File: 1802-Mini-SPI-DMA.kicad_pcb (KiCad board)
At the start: 2 copper layers, 100 x 100 mm, 44 parts, among them J1 Conn_02x05_Odd_Even, J2 Mount, J3 Mount, J4 Mount, J5 GRP_EXP, J6 Mount, J7 Conn_01x08, J8 GRP_SEL, J9 Expansion, U1 74HC04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

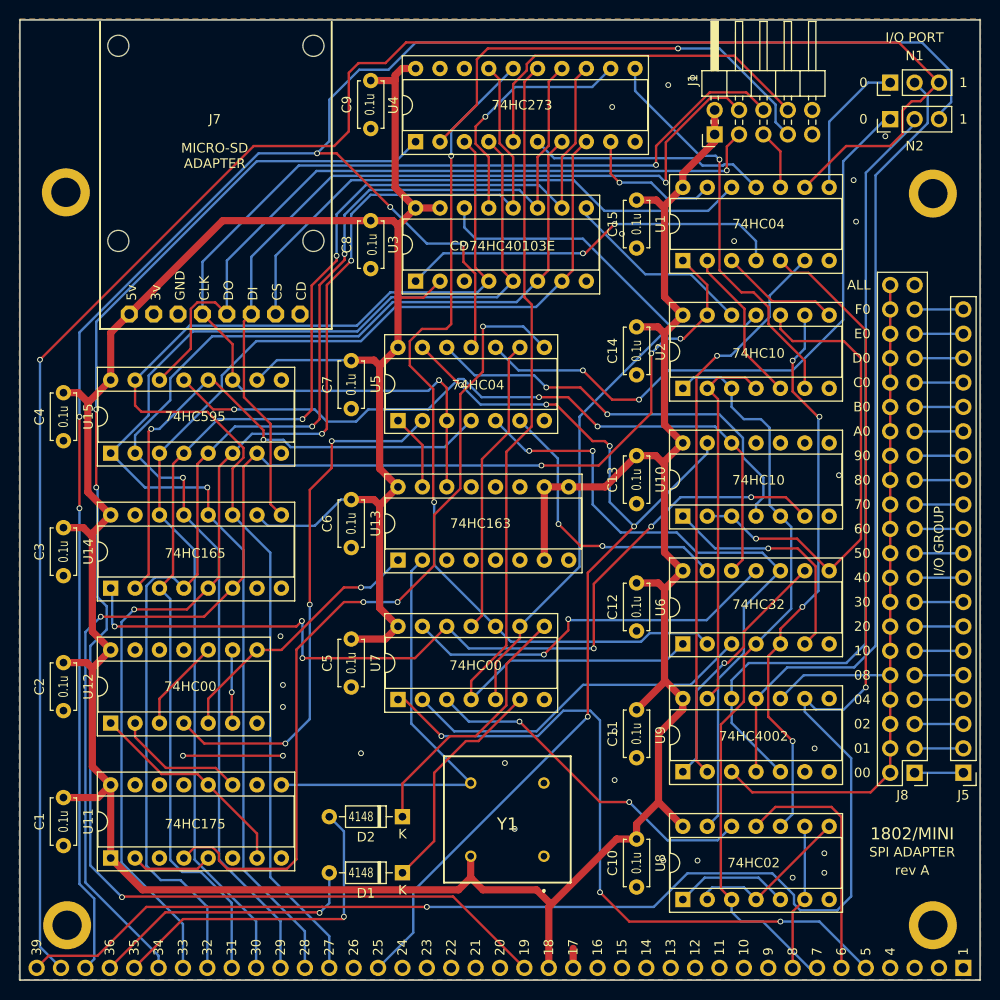
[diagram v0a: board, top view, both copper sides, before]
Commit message: Update silk screen.
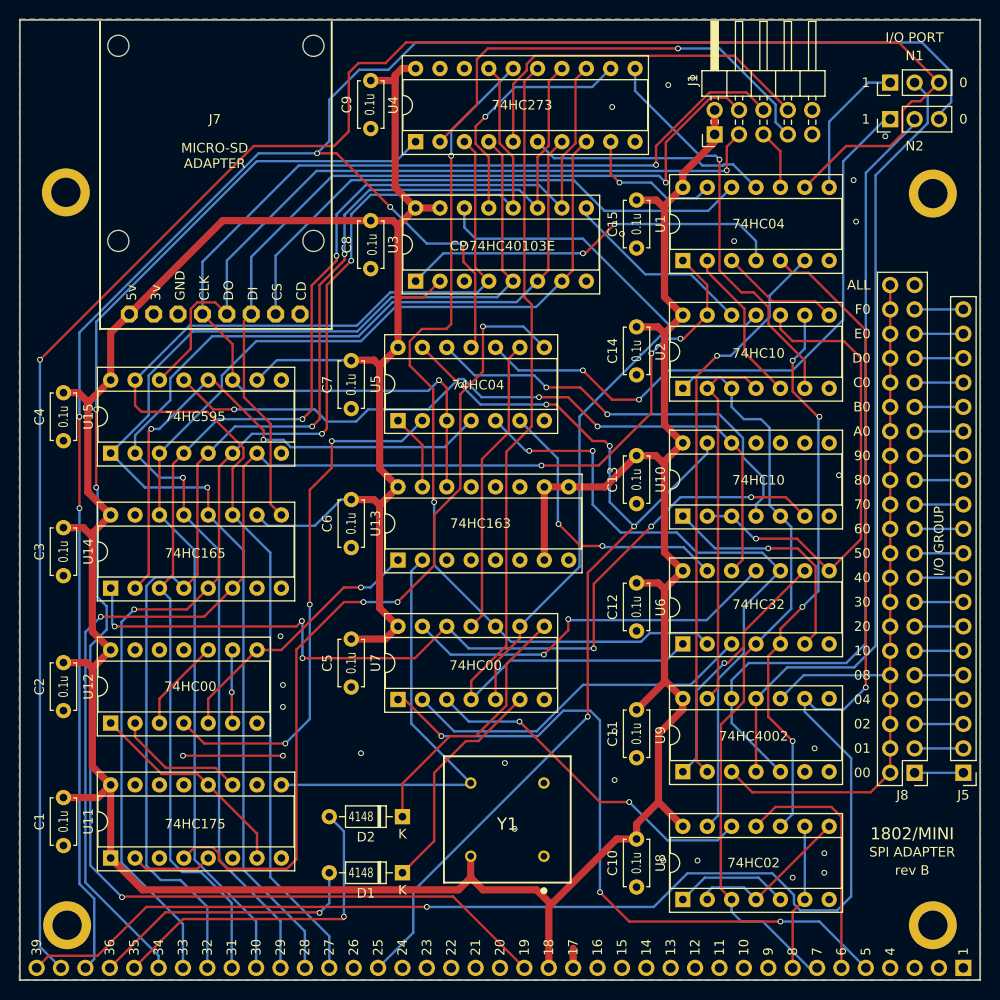
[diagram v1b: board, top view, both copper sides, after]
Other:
- board text added: "rev B"
- board text removed: "rev A"
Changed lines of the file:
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@@
   (gr_line (start 132.334 79.502) (end 132.334 47.498) (layer "F.SilkS") (width 0.2))
   (gr_line (start 108.204 79.502) (end 132.334 79.502) (layer "F.SilkS") (width 0.2))
+  (gr_circle (center 154.432 138.019) (end 154.686 137.922) (layer "F.SilkS") (width 0.2) (fill none))
   (gr_line (start 108.204 47.498) (end 108.204 79.502) (layer "F.SilkS") (width 0.2))
   (gr_rect (start 99.86 47.32) (end 199.86 147.32) (layer "Edge.Cuts") (width 0.15) (fill none))
@@
     (effects (font (size 1 1) (thickness 0.15)) (justify mirror))
   )
-  (gr_text "1" (at 197.612 53.848) (layer "B.SilkS")
+  (gr_text "1" (at 187.452 53.848) (layer "B.SilkS")
     (effects (font (size 1 1) (thickness 0.15)) (justify right mirror))
   )
@@
     (effects (font (size 1 1) (thickness 0.15)) (justify mirror))
   )
-  (gr_text "0" (at 188.214 57.658) (layer "B.SilkS")
+  (gr_text "0" (at 198.628 57.658) (layer "B.SilkS")
     (effects (font (size 1 1) (thickness 0.15)) (justify left mirror))
   )
@@
     (effects (font (size 1 1) (thickness 0.15)) (justify mirror))
   )
-  (gr_text "0" (at 188.214 53.848) (layer "B.SilkS")
+  (gr_text "0" (at 198.628 53.848) (layer "B.SilkS")
     (effects (font (size 1 1) (thickness 0.15)) (justify left mirror))
   )
@@
     (effects (font (size 1 0.7) (thickness 0.12)) (justify mirror))
   )
-  (gr_text "1" (at 197.612 57.658) (layer "B.SilkS")
+  (gr_text "1" (at 187.452 57.658) (layer "B.SilkS")
     (effects (font (size 1 1) (thickness 0.15)) (justify right mirror))
   )
@@
     (effects (font (size 1 1) (thickness 0.15)) (justify left))
   )
-  (gr_text "1" (at 198.12 57.658) (layer "F.SilkS")
+  (gr_text "1" (at 187.96 57.658) (layer "F.SilkS")
     (effects (font (size 1 1) (thickness 0.15)))
   )
@@
     (effects (font (size 1 1) (thickness 0.15)))
   )
-  (gr_text "rev A" (at 192.786 135.89) (layer "F.SilkS")
+  (gr_text "rev B" (at 192.786 135.89) (layer "F.SilkS")
     (effects (font (size 1 1) (thickness 0.15)))
   )
@@
     (effects (font (size 1 1) (thickness 0.15)) (justify right))
   )
-  (gr_text "1" (at 198.12 53.848) (layer "F.SilkS")
+  (gr_text "1" (at 187.96 53.848) (layer "F.SilkS")
     (effects (font (size 1 1) (thickness 0.15)))
   )
@@
     (effects (font (size 1 1) (thickness 0.15)) (justify right))
   )
-  (gr_text "0" (at 187.706 57.658) (layer "F.SilkS")
+  (gr_text "0" (at 198.12 57.658) (layer "F.SilkS")
     (effects (font (size 1 1) (thickness 0.15)))
   )
@@
     (effects (font (size 1 1) (thickness 0.15)))
   )
-  (gr_text "0" (at 187.706 53.848) (layer "F.SilkS")
-    (effects (font (size 1 1) (thickness 0.15)))
-  )
+  (gr_text "0" (at 198.12 53.848) (layer "F.SilkS")
+    (effects (font (size 1 1) (thickness 0.15)))
+  )
